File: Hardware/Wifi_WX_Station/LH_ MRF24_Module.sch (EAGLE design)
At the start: 7 parts, among them M1 MRF24WB0MA

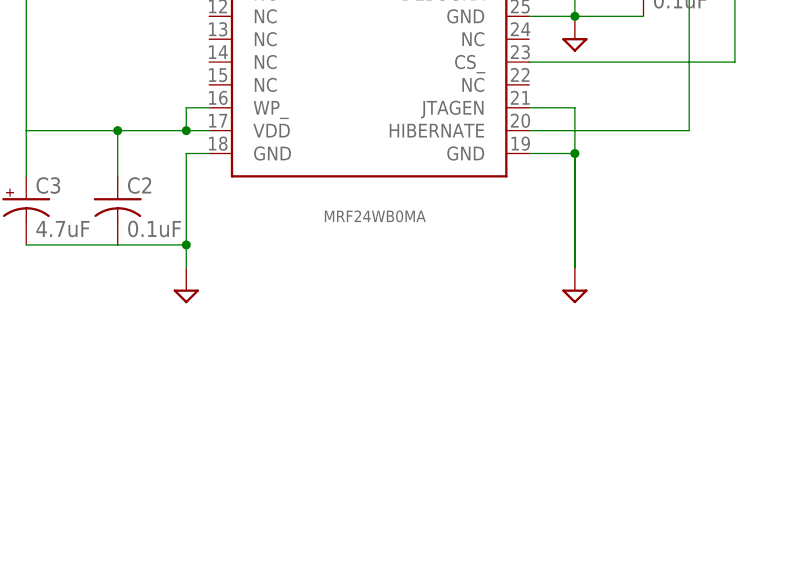
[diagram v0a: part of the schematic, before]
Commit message: Modified the RF carrier slightly with longer pads for easier soldering.
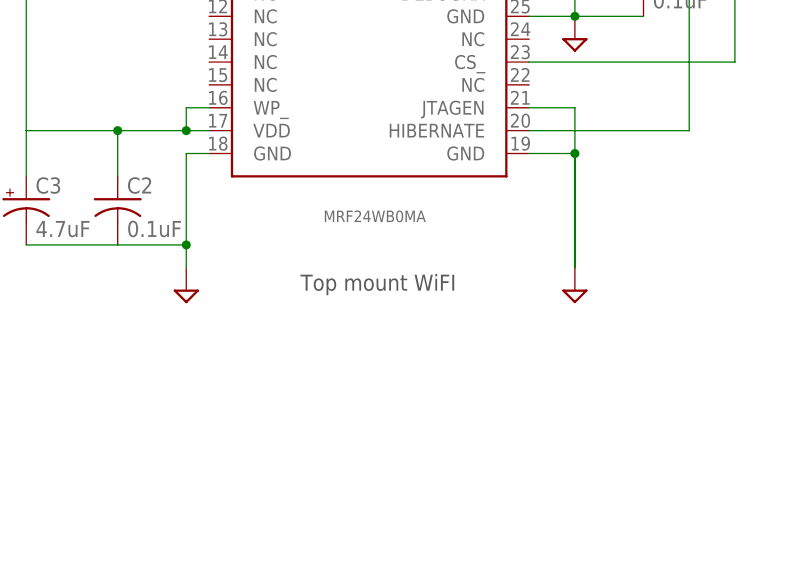
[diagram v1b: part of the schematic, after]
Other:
- note added: "Top mount WiFI"
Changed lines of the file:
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@@
 <?xml version="1.0" encoding="utf-8"?>
 <!DOCTYPE eagle SYSTEM "eagle.dtd">
-<eagle version="6.3">
+<eagle version="6.5.0">
 <drawing>
 <settings>
@@
 <text x="109.22" y="-30.48" size="5.08" layer="94" ratio="20">WunderWxStation</text>
 <text x="176.784" y="-49.276" size="3.81" layer="94" ratio="20">B.2</text>
+<text x="22.86" y="-5.08" size="1.778" layer="97">Top mount WiFI</text>
 </plain>
 <instances>
